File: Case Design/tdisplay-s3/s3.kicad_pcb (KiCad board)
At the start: 2 copper layers, 34 x 109.9 mm, 13 parts, among them SW6 SW_PUSH_6mm_H9.5mm, SW7 SW_PUSH_6mm_H9.5mm, SW8 SW_PUSH_6mm_H9.5mm

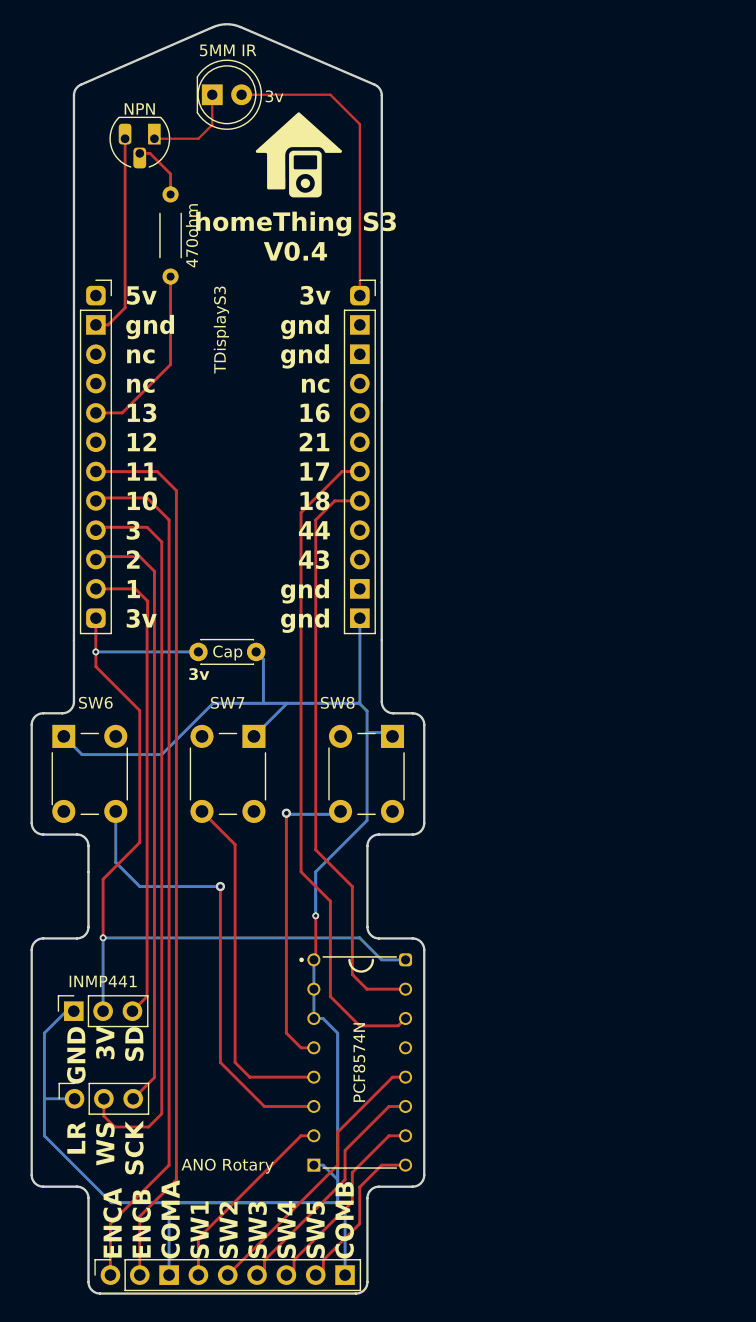
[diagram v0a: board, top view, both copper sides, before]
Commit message: add charge and data port to pcb (#130)
* add charge and data port to pcb

* update pcb image
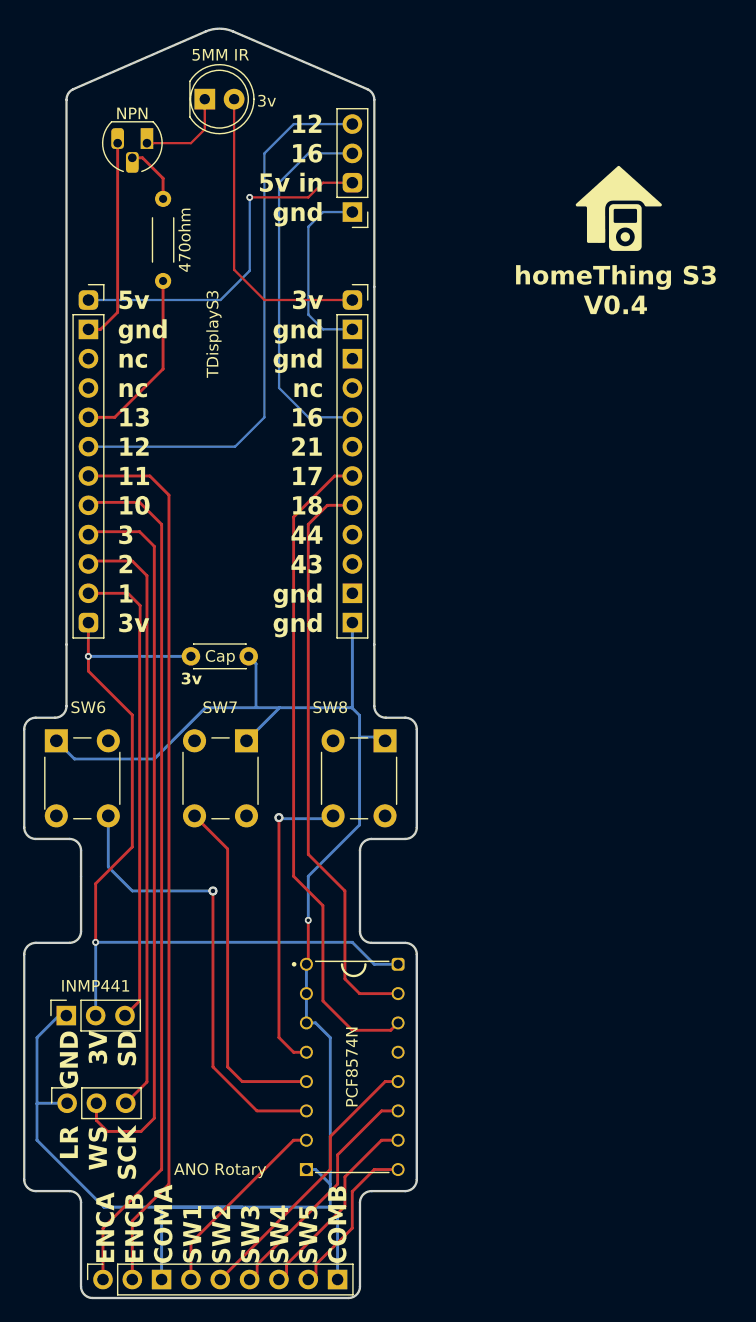
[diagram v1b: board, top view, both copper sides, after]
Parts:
- added REF**: PinHeader_1x04_P2.54mm_Vertical, Connector_PinHeader_2.54mm:PinHeader_1x04_P2.54mm_Vertical, F.Cu at (221.0, 58.4)
- moved INMP441 2 0.75 mm to (196.3, 135.6)
- moved 470ohm 0.75 mm to (204.6, 63.4)
- moved 5MM IR 0.75 mm to (208.2, 48.6)
- moved Cap 0.75 mm to (207.0, 96.9)
- moved INMP441 0.75 mm to (196.2, 128.0)
- moved REF** 0.75 mm to (221.0, 66.0)
- moved SW6 0.75 mm to (195.3, 110.7)
- moved TDisplayS3 0.75 mm to (198.1, 66.0)
- moved NPN 0.75 mm to (203.2, 52.5)
- moved ANO Rotary 0.75 mm to (199.4, 150.9)
- moved PCF8574N 0.75 mm to (221.0, 132.5)
- moved SW8 0.75 mm to (219.3, 110.7)
- moved SW7 0.75 mm to (207.3, 110.7)
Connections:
- REF** pad 2: (no net) -> ground3
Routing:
- net 12: track 0.00 -> 47.8 mm
- net 16: track 0.00 -> 32.6 mm
- net 5v: track 0.00 -> 30.8 mm, vias 0 -> 1
- net ground3: track 0.00 -> 16.3 mm
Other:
- board text added: "12 16 5v in gnd"
